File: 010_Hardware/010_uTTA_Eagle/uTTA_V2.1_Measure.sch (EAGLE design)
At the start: 286 parts, among them IC101.1 LT1167, IC101.2 LT1167, IC101.3 LT1167, IC101.4 LT1167, IC151.1 MCP602SN, IC151.3 MCP602SN, IC301 AD5664, IC302 LT1004CLP-2.5, IC303 TL074D, IC351.1 AD8672ARZ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

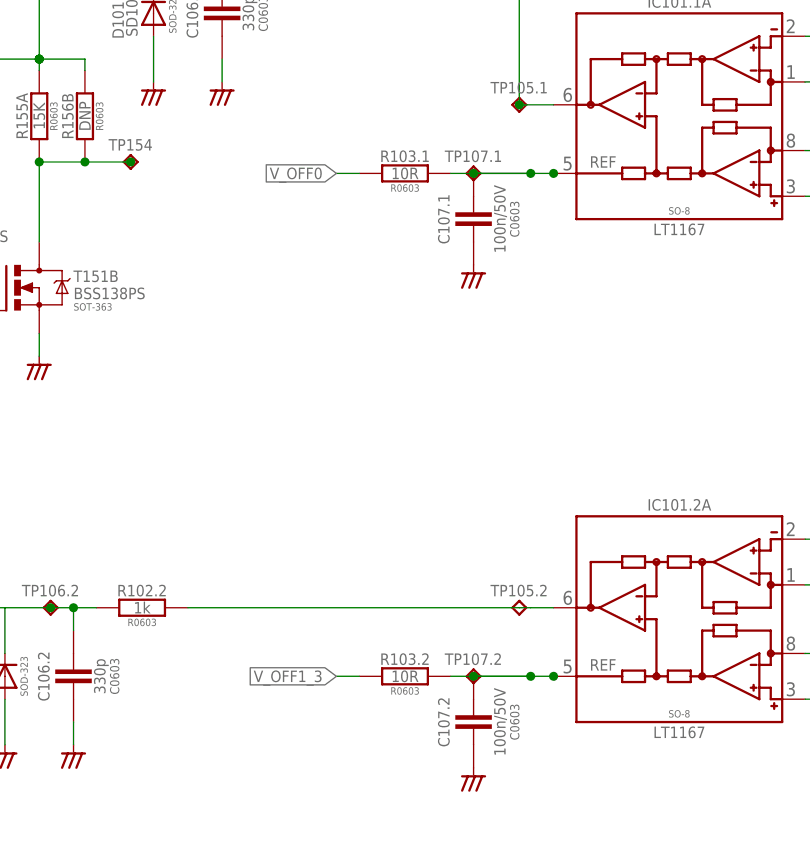
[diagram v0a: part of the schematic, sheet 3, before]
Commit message: Change of Offset Voltage decoupling resistors
Changed decoupling resistors from 10 Ohm to 0Ohm to reduce incluence on measurement results
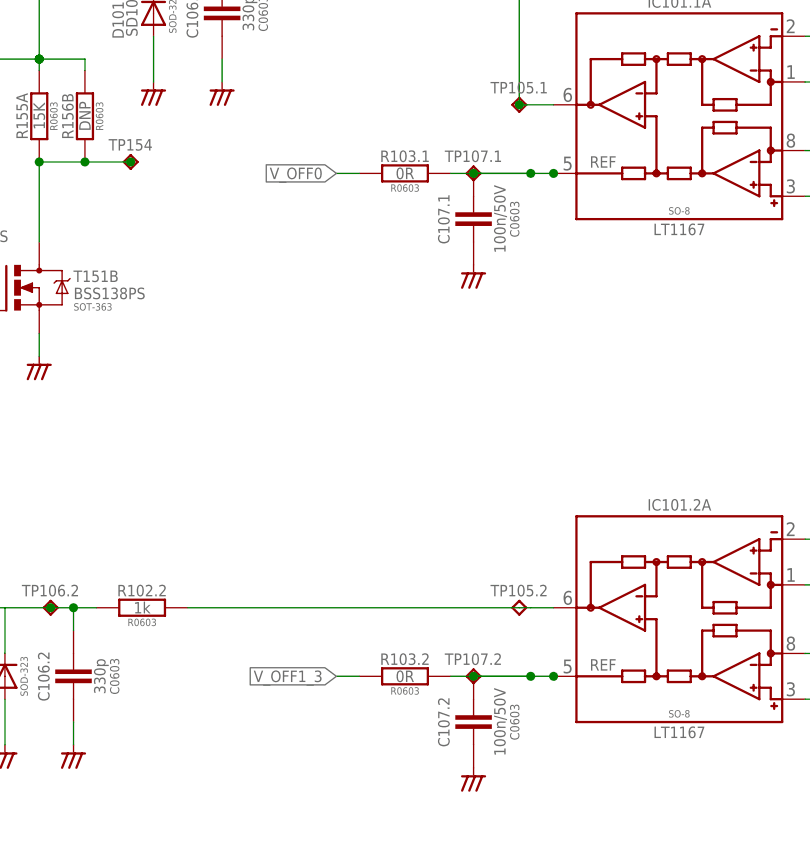
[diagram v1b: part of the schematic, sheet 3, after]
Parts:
- R103.1, R103.2, R103.3, R103.4: value 10R -> 0R
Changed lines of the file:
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@@
 <attribute name="TOLERANCE" value="0.1%"/>
 </part>
-<part name="R103.1" library="A_Resistor" deviceset="R-EU_" device="R0603" value="10R"/>
+<part name="R103.1" library="A_Resistor" deviceset="R-EU_" device="R0603" value="0R"/>
 <part name="R321.1" library="A_Resistor" deviceset="R-EU_" device="R0603" value="10k">
 <attribute name="TOLERANCE" value="0.1%"/>
@@
 <attribute name="TOLERANCE" value="0.1%"/>
 </part>
-<part name="R103.2" library="A_Resistor" deviceset="R-EU_" device="R0603" value="10R"/>
+<part name="R103.2" library="A_Resistor" deviceset="R-EU_" device="R0603" value="0R"/>
 <part name="L101.2" library="A_Ferrite" deviceset="FB" device="MMZ2012S" value="FBMMZ2012S">
 <attribute name="PACKAGE" value="2012"/>
@@
 <attribute name="TOLERANCE" value="0.1%"/>
 </part>
-<part name="R103.3" library="A_Resistor" deviceset="R-EU_" device="R0603" value="10R"/>
+<part name="R103.3" library="A_Resistor" deviceset="R-EU_" device="R0603" value="0R"/>
 <part name="L101.3" library="A_Ferrite" deviceset="FB" device="MMZ2012S" value="FBMMZ2012S">
 <attribute name="PACKAGE" value="2012"/>
@@
 <variant name="Controller Adjust" populate="no"/>
 </part>
-<part name="R103.4" library="A_Resistor" deviceset="R-EU_" device="R0603" value="10R">
+<part name="R103.4" library="A_Resistor" deviceset="R-EU_" device="R0603" value="0R">
 <variant name="Manual_Adjust" populate="no"/>
 </part>

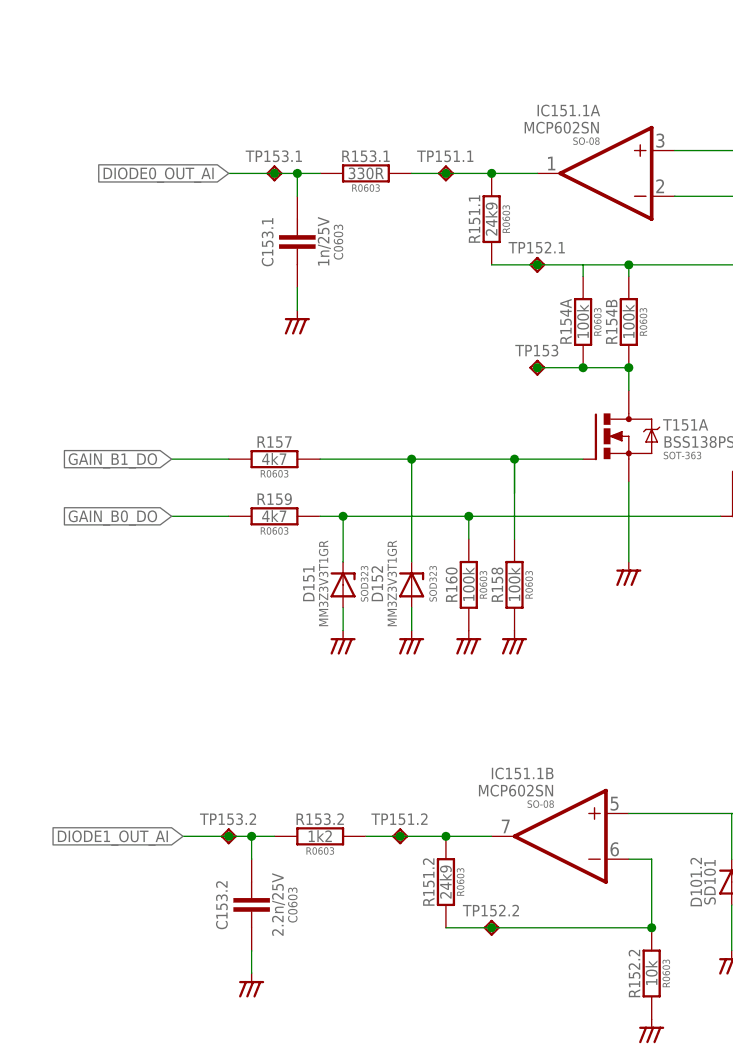
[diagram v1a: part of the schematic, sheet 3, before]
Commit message: Update of ADC filter RC-values
Changed ADC filter values to reduce effect of sampling droop
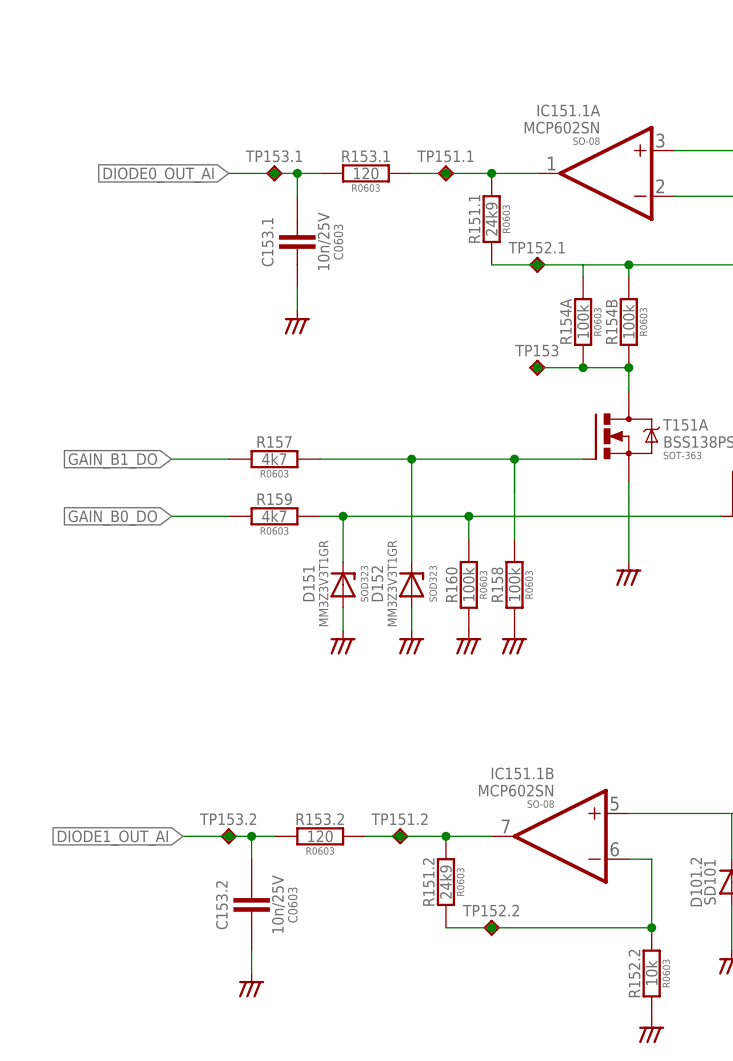
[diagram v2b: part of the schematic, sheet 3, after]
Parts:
- C153.1: value 1n/25V -> 10n/25V
- C153.2, C153.3, C153.4: value 2.2n/25V -> 10n/25V
- R153.1: value 330R -> 120
- R153.2, R153.3, R153.4: value 1k2 -> 120
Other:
- note added: "tau = 1.2µs fc = 132.6kHz"
- note removed: "tau = 2.64µs fc = 60.2kHz"
- note removed: "tau = 330ns fc = 1.461MHz"
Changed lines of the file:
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@@
 <part name="C306" library="A_Kondensatoren" deviceset="C-EU" device="C0603" value="100n/50V"/>
 <part name="AGND15" library="supply" deviceset="AGND_" device=""/>
-<part name="R153.1" library="A_Resistor" deviceset="R-EU_" device="R0603" value="330R"/>
+<part name="R153.1" library="A_Resistor" deviceset="R-EU_" device="R0603" value="120"/>
 <part name="C107.1" library="A_Kondensatoren" deviceset="C-EU" device="C0603" value="100n/50V"/>
 <part name="AGND7" library="supply" deviceset="AGND_" device=""/>
@@
 </part>
 <part name="C105.2" library="A_Kondensatoren" deviceset="C-EU" device="C0603" value="10p"/>
-<part name="R153.2" library="A_Resistor" deviceset="R-EU_" device="R0603" value="1k2"/>
+<part name="R153.2" library="A_Resistor" deviceset="R-EU_" device="R0603" value="120"/>
 <part name="C107.2" library="A_Kondensatoren" deviceset="C-EU" device="C0603" value="100n/50V"/>
 <part name="AGND14" library="supply" deviceset="AGND_" device=""/>
@@
 </part>
 <part name="C105.3" library="A_Kondensatoren" deviceset="C-EU" device="C0603" value="10p"/>
-<part name="R153.3" library="A_Resistor" deviceset="R-EU_" device="R0603" value="1k2"/>
+<part name="R153.3" library="A_Resistor" deviceset="R-EU_" device="R0603" value="120"/>
 <part name="C107.3" library="A_Kondensatoren" deviceset="C-EU" device="C0603" value="100n/50V"/>
 <part name="AGND17" library="supply" deviceset="AGND_" device=""/>
@@
 <variant name="Controller Adjust" populate="no"/>
 </part>
-<part name="R153.4" library="A_Resistor" deviceset="R-EU_" device="R0603" value="1k2">
+<part name="R153.4" library="A_Resistor" deviceset="R-EU_" device="R0603" value="120">
 <variant name="Manual_Adjust" populate="no"/>
 <variant name="Controller Adjust" populate="no"/>
@@
 <attribute name="PACKAGE" value="R0603"/>
 </part>
-<part name="C153.3" library="A_Kondensatoren" deviceset="C-EU" device="C0603" value="2.2n/25V">
+<part name="C153.3" library="A_Kondensatoren" deviceset="C-EU" device="C0603" value="10n/25V">
 <attribute name="PACKAGE" value="C0603"/>
 </part>
-<part name="C153.4" library="A_Kondensatoren" deviceset="C-EU" device="C0603" value="2.2n/25V">
+<part name="C153.4" library="A_Kondensatoren" deviceset="C-EU" device="C0603" value="10n/25V">
 <attribute name="PACKAGE" value="C0603"/>
 <variant name="Manual_Adjust" populate="no"/>
 <variant name="Controller Adjust" populate="no"/>
 </part>
-<part name="C153.2" library="A_Kondensatoren" deviceset="C-EU" device="C0603" value="2.2n/25V">
+<part name="C153.2" library="A_Kondensatoren" deviceset="C-EU" device="C0603" value="10n/25V">
 <attribute name="PACKAGE" value="C0603"/>
 </part>
-<part name="C153.1" library="A_Kondensatoren" deviceset="C-EU" device="C0603" value="1n/25V">
+<part name="C153.1" library="A_Kondensatoren" deviceset="C-EU" device="C0603" value="10n/25V">
 <attribute name="PACKAGE" value="C0603"/>
 </part>
@@
 INA128:  G= (50k/Rg)+1</text>
 <text x="142.24" y="119.38" size="1.27" layer="98">Vout = (V_IN,P - V_IN,N)*G + V_REF</text>
-<text x="45.085" y="99.695" size="1.27" layer="98" ratio="14">tau = 330ns
-fc = 1.461MHz</text>
-<text x="40.64" y="26.035" size="1.27" layer="98" ratio="14">tau = 2.64µs
-fc = 60.2kHz</text>
+<text x="45.085" y="99.695" size="1.27" layer="98" ratio="14">tau = 1.2µs
+fc = 132.6kHz</text>
+<text x="40.64" y="26.035" size="1.27" layer="98" ratio="14">tau = 1.2µs
+fc = 132.6kHz</text>
 <wire x1="3.81" y1="60.96" x2="113.03" y2="60.96" width="0.4064" layer="98"/>
 <wire x1="113.03" y1="60.96" x2="113.03" y2="67.31" width="0.4064" layer="98"/>
@@
 <text x="154.94" y="82.55" size="1.778" layer="98">LT1167:  G= (49k4/Rg)+1
 INA128:  G= (50k/Rg)+1</text>
-<text x="40.64" y="84.455" size="1.27" layer="98" ratio="14">tau = 2.64µs
-fc = 60.2kHz</text>
-<text x="40.64" y="28.575" size="1.27" layer="98" ratio="14">tau = 2.64µs
-fc = 60.2kHz</text>
+<text x="40.64" y="84.455" size="1.27" layer="98" ratio="14">tau = 1.2µs
+fc = 132.6kHz</text>
+<text x="40.64" y="28.575" size="1.27" layer="98" ratio="14">tau = 1.2µs
+fc = 132.6kHz</text>
 <wire x1="3.81" y1="132.08" x2="256.54" y2="132.08" width="0.4064" layer="98"/>
 <wire x1="3.81" y1="69.85" x2="256.54" y2="69.85" width="0.4064" layer="98"/>
